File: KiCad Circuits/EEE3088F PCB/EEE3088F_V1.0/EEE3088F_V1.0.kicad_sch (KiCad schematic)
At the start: 45 parts, among them J1 Conn_01x02_Pin, J2 Conn_02x16_Odd_Even, U1 MT3608, U2 INA219AxD, U3 DRV8833PWP, U4 AP2112K-3.3, U5 DRV8833PWP, U6 BQ24074RGT, U7 AP2171W, U8 AP2171W

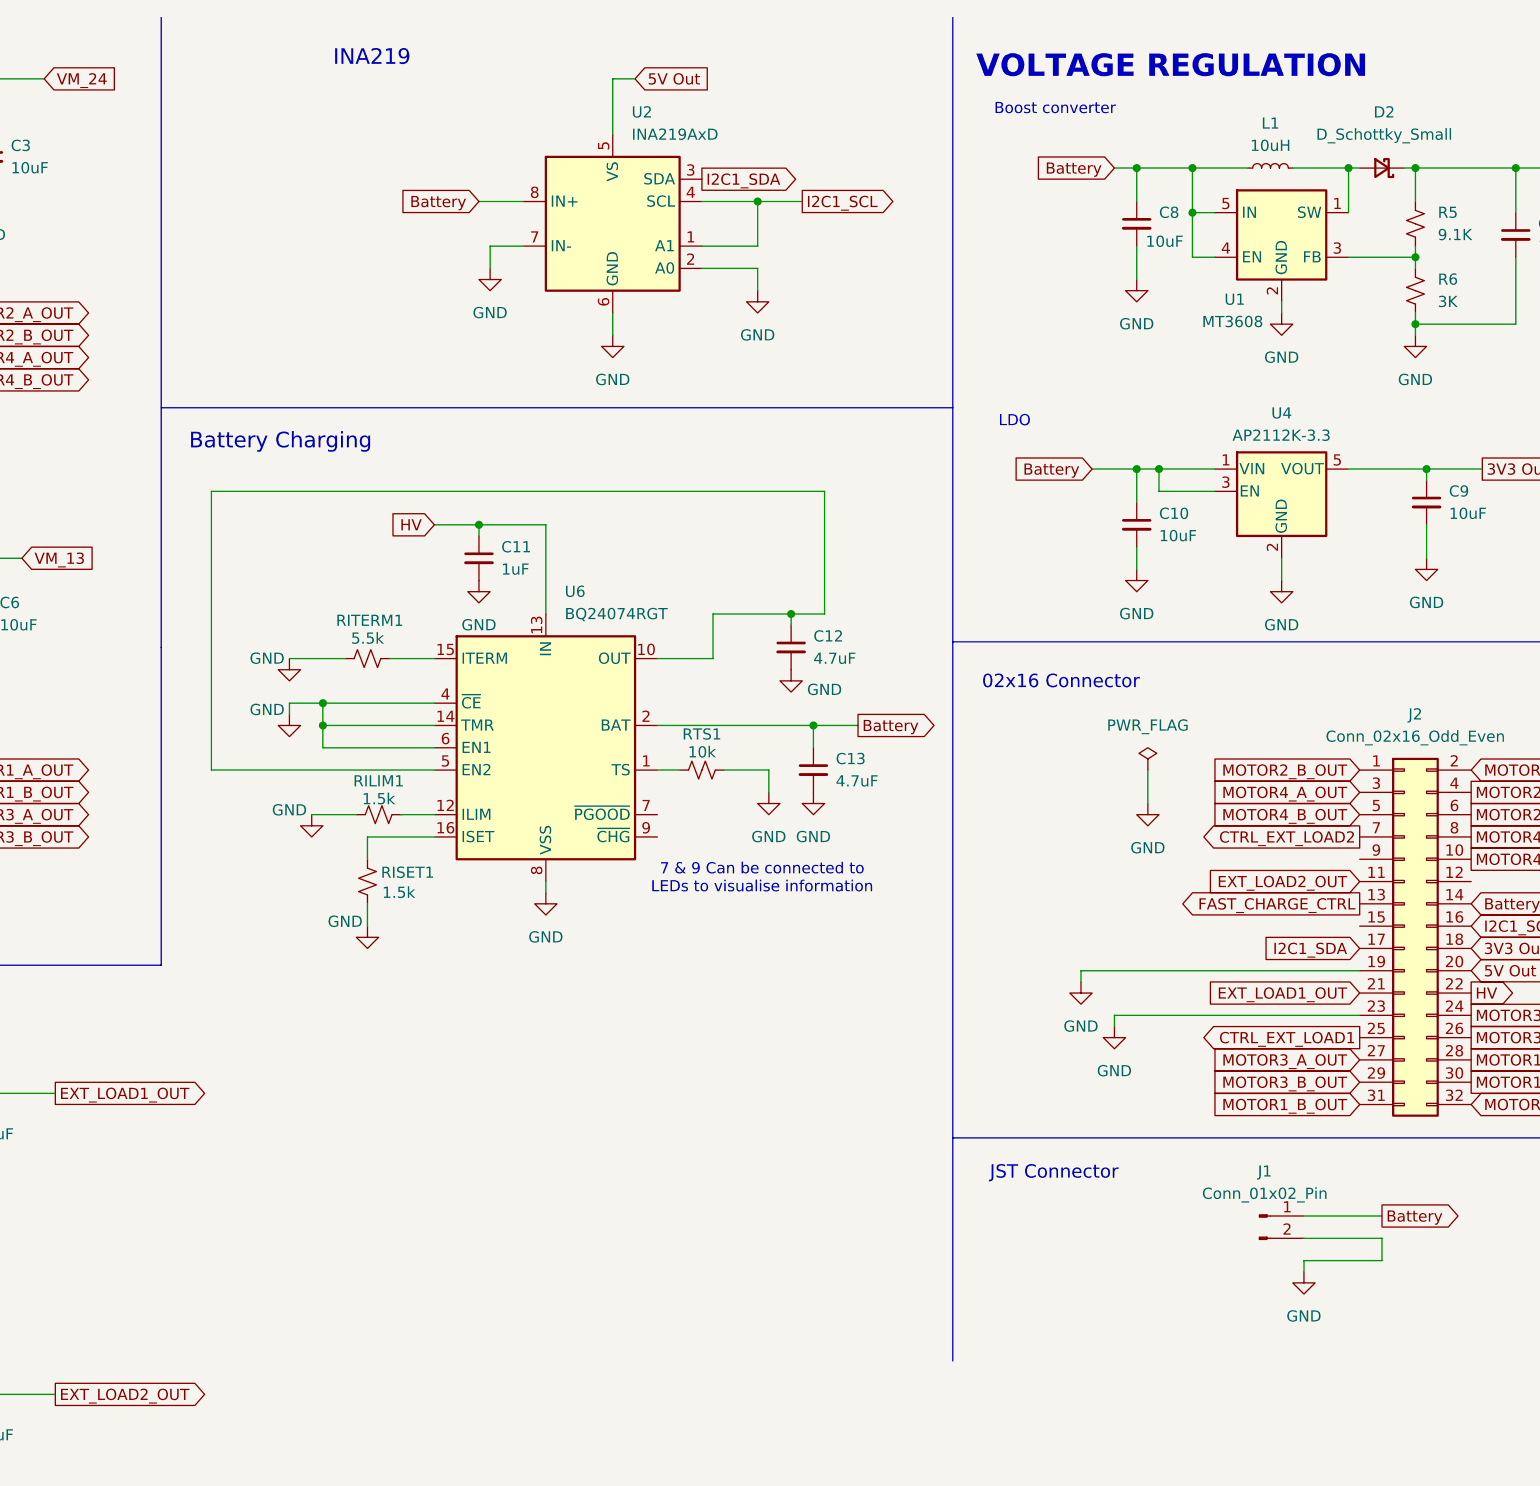
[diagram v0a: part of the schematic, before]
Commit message: added INA219
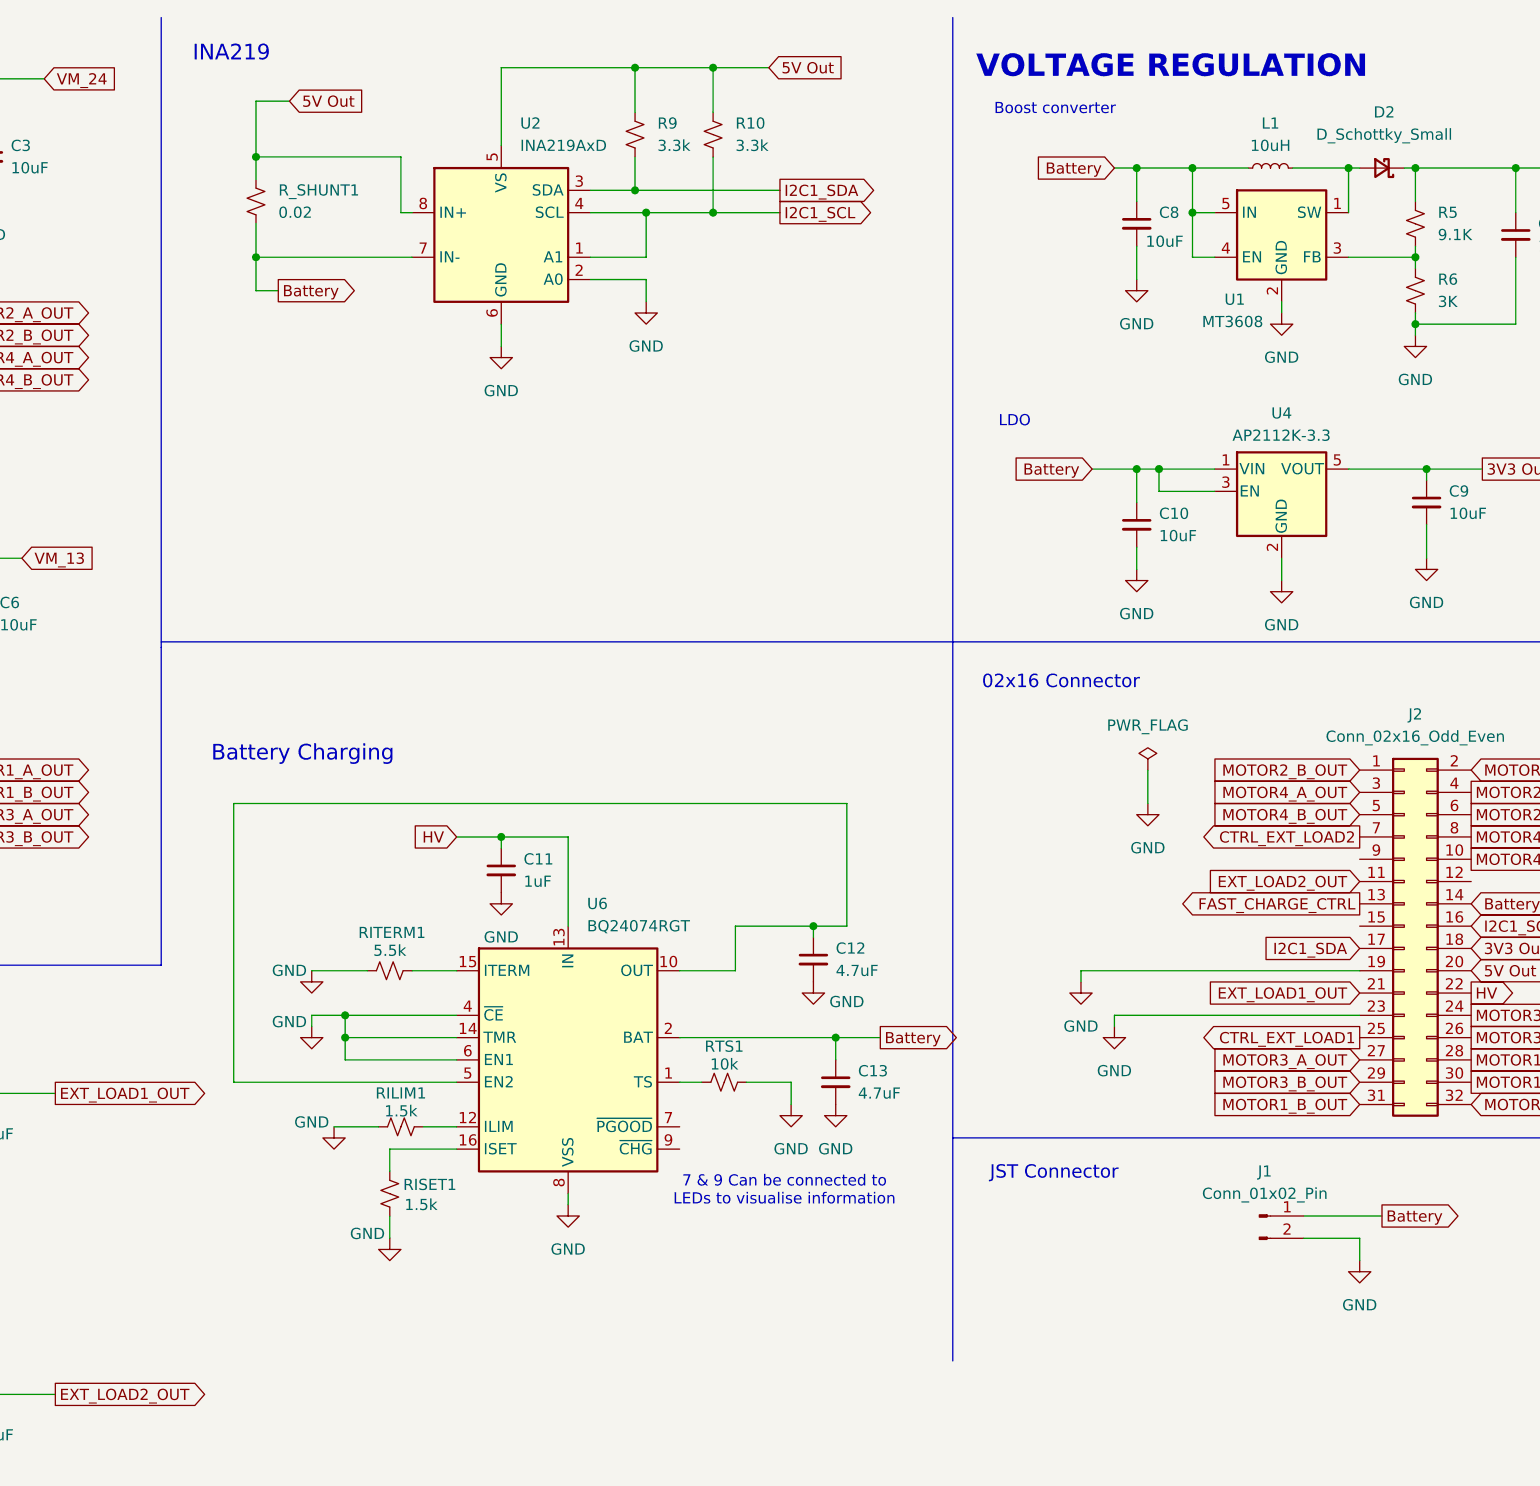
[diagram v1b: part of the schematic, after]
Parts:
- added R10, R9: 3.3k, symbol Device:R_Small_US
- added R_SHUNT1: 0.02, symbol Device:R_Small_US
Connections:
- net 5V Out: now also U2.8 (IN+), R10.1, R9.1, R_SHUNT1.1
- net Battery: now also U2.7 (IN-), R_SHUNT1.2; no longer U2.8 (IN+)
- net GND: no longer U2.7 (IN-)
- net I2C1_SCL: now also R10.2
- net I2C1_SDA: now also R9.2
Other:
- moved on the sheet: C11, C12, C13, RILIM1, RISET1, RITERM1, RTS1, U2, U6

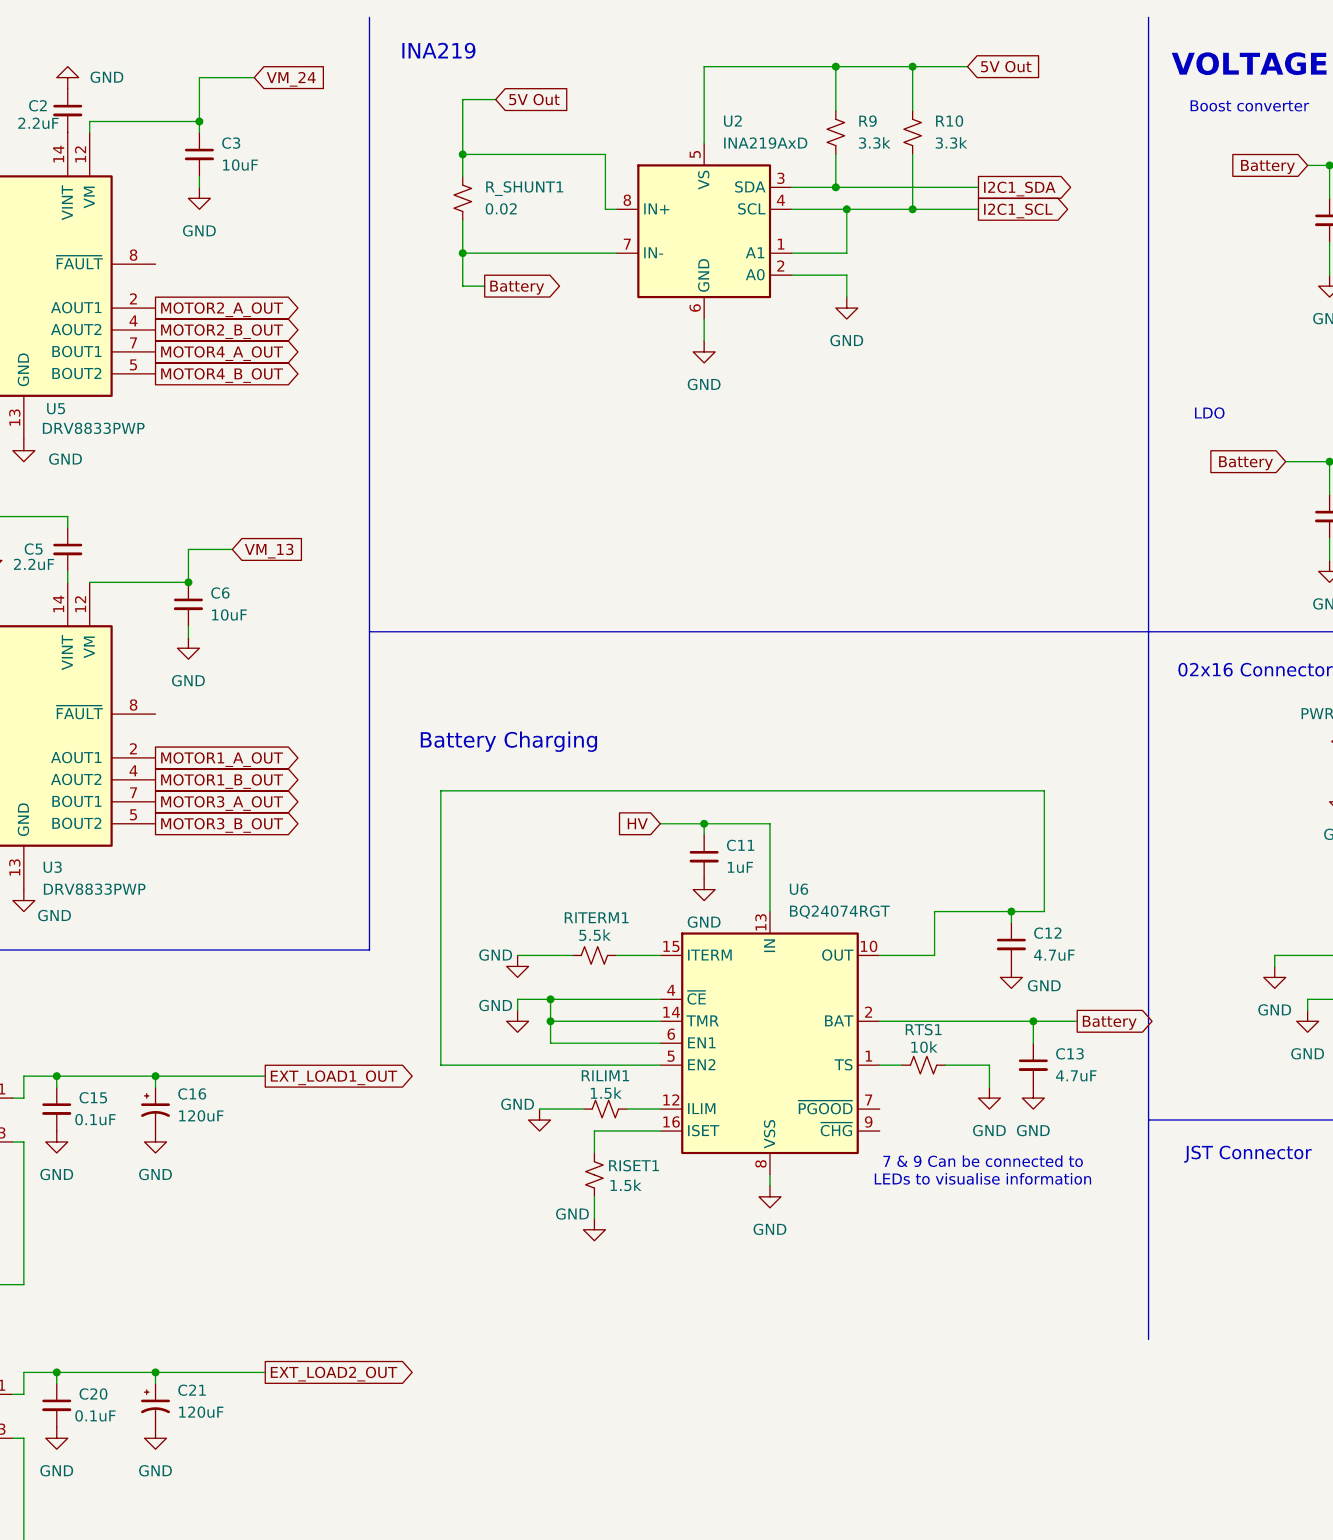
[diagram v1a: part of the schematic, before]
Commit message: added footprints folder
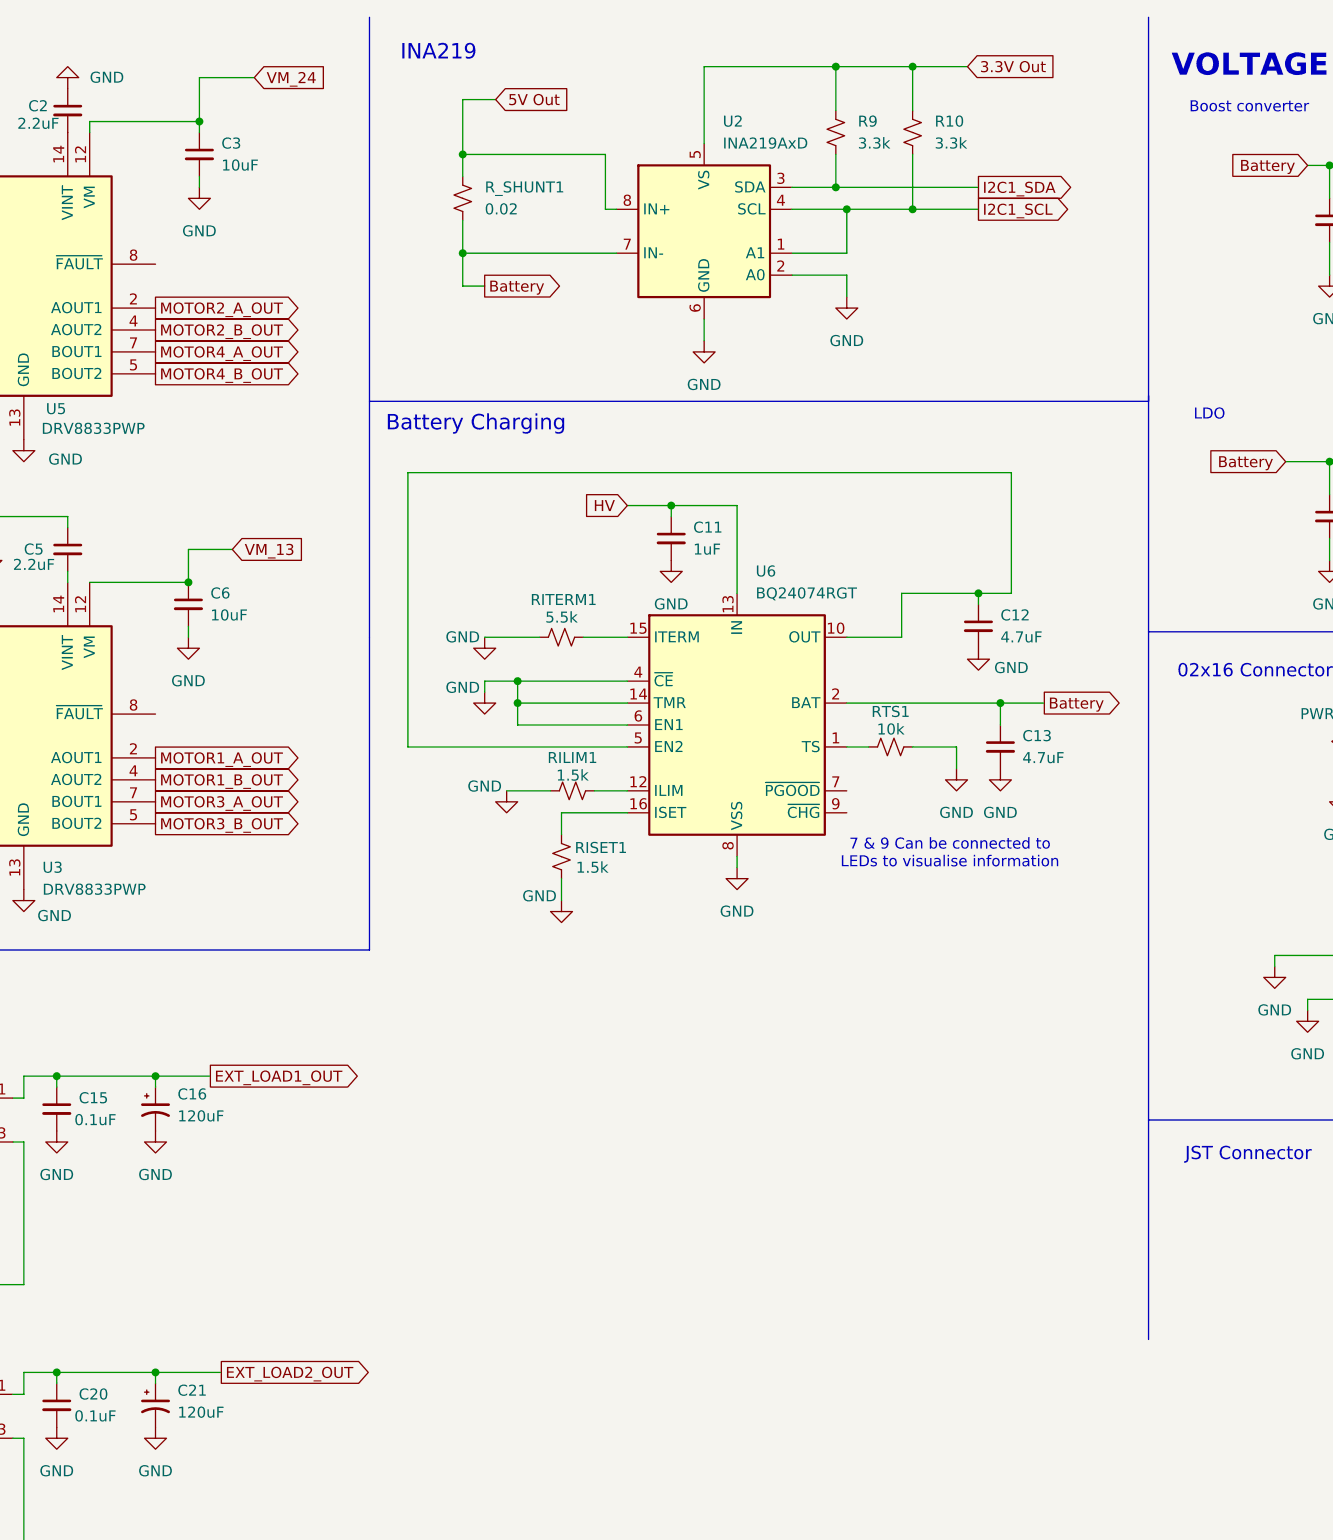
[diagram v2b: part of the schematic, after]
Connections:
- net 5V Out: no longer R10.1, R9.1, U2.5 (VS)
- new net 3.3V Out: R10.1, R9.1, U2.5 (VS)
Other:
- moved on the sheet: C11, C12, C13, RILIM1, RISET1, RITERM1, RTS1, U6
